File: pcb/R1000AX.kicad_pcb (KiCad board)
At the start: 4 copper layers, 175 x 65.5 mm, 133 parts, among them J1 PCIESOCKET-X1, J10 PCIESOCKET-X1, J11 PCIESOCKET-X1, J12 PCIESOCKET-X1, J13 PCIESOCKET-X1, J14 PCIESOCKET-X1, J15 PCIESOCKET-X1, J16 CONN127P-02X05, J17 USB_B_RECEPTACLE, J18 SOCKET254P-01X02, J2 PCIESOCKET-X1, J25 SOCKET420P-02X04-CPU, J3 PCIESOCKET-X1, J31 USB_A_RECEPTACLE_2, J4 PCIESOCKET-X1, J5 PCIESOCKET-X1, J6 PCIESOCKET-X1, J7 PCIESOCKET-X1, J8 PCIESOCKET-X1, J81 SOCKET254P-01X02, J82 SOCKET254P-01X02, J83 SOCKET254P-01X02, J9 PCIESOCKET-X1, Q1 DMG2305UX-7, Q2 PSMN1R2-30YLC, Q3 Q_PNP_BEC, Q4 Q_NPN_BEC, Q5 Q_PNP_BEC, Q6 Q_PNP_BEC, U1 LPC1769FBD100,551, U2 AP3418, U20 M24C08-FDW6TP, U3 BD9E302EFJ-E2, U4 INA3221AIRGVR, U5 LM5060MM/NOPB, Y1 XTAL4_12MHz

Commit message: updated silkscreen with RoHS
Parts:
- added A5: ART, Symbols:RoHS-Logo_6mm_SilkScreen, B.Cu at (165.4, 93.6)
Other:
- board text added: "EEPROM WRITE PROT"

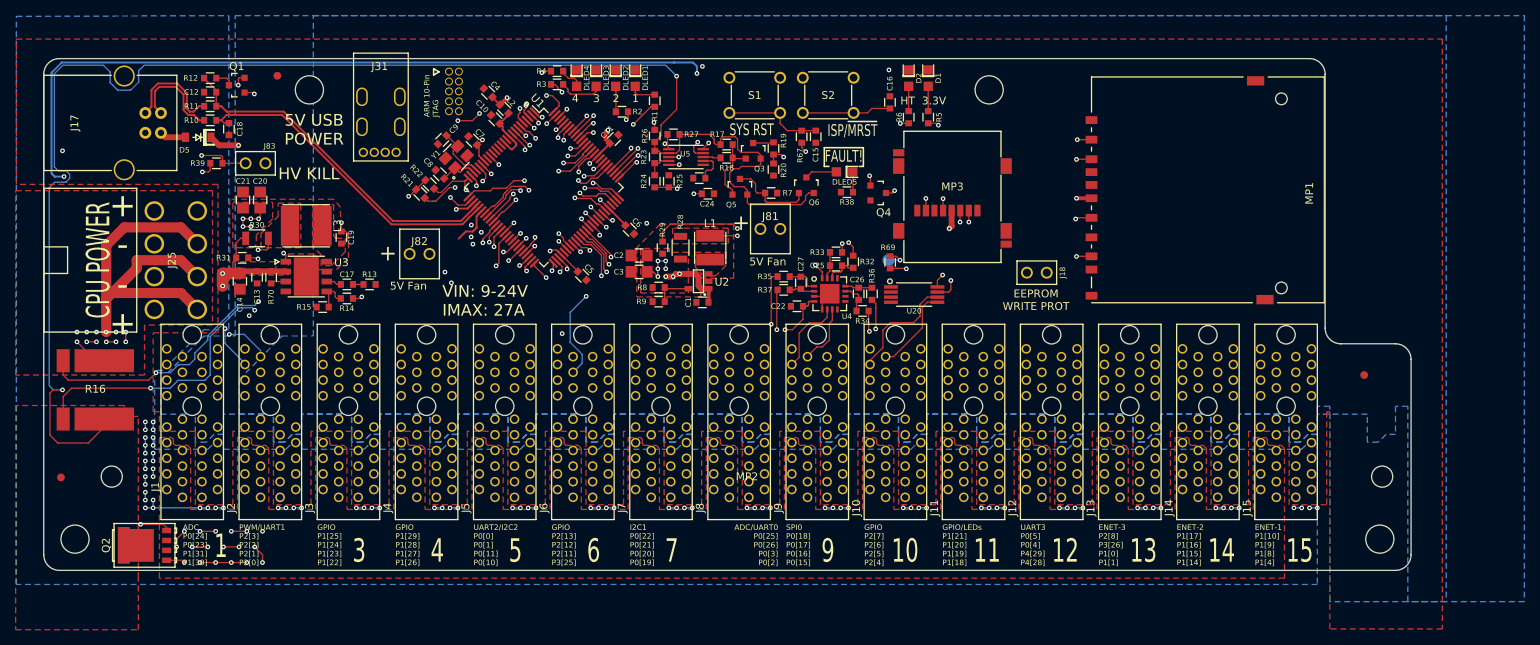
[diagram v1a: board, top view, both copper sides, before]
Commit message: added socket for CHIP and other compute modules
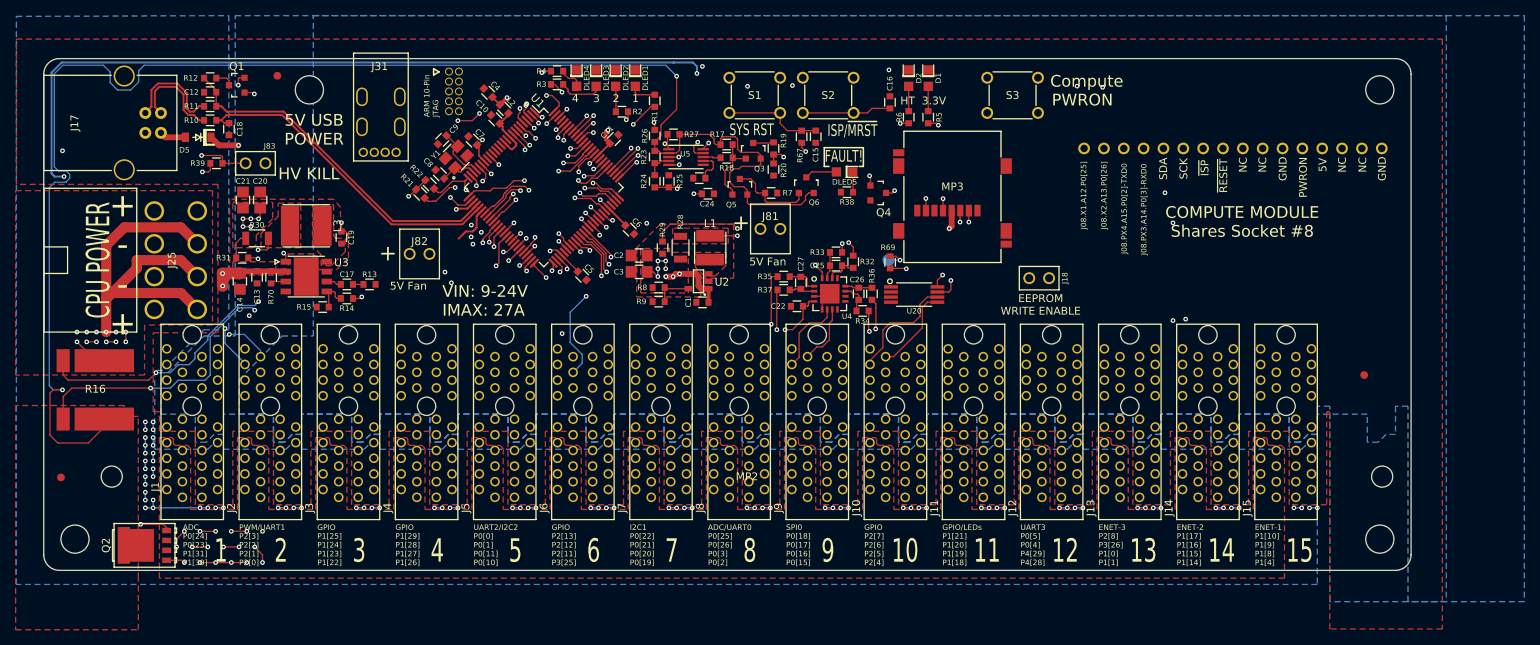
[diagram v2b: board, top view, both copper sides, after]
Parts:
- removed MP1: SDCARD_RECEPTACLE, Main:SDCARD_RECEPTACLE
- added J19: CHIPPRO, Main:CHIPPRO, F.Cu at (203.2, 85.0)
- added S3: SPST_PUSHBTN, Main:SPST_PUSHBTN, F.Cu at (175.0, 78.2)
- moved MP8 50.5 mm to (221.8, 85.8)
- moved A5 47.6 mm to (211.8, 104.0)
- moved A3 19.2 mm to (217.8, 94.0)
- moved A4 11.0 mm to (175.8, 93.2)
- moved A1 10.1 mm to (197.0, 94.0)
- moved J18 0.76 mm to (178.4, 101.6)
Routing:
- net J08.PX2.A13.P0[26]: track 63.3 -> 152.6 mm, vias 1 -> 2
- net J08.PX3.A14.P0[3]: track 60.7 -> 148.0 mm
- net J08.PX1.A12.P0[25]: track 63.9 -> 150.2 mm, vias 1 -> 2
- net /~RESET: track 48.9 -> 131.5 mm, vias 1 -> 2
- net J08.PX4.A15.P0[2]: track 65.1 -> 146.3 mm
- net ~MRESET: track 272.2 -> 329.1 mm, vias 3 -> 4
- net /PWRON: track 0.00 -> 48.4 mm
- net SCL0: track 253.9 -> 283.6 mm, vias 3 -> 5
- net SDA0: track 228.9 -> 258.3 mm, vias 2 -> 4
- net SD_SSEL: track 83.4 -> 59.0 mm, vias 3 -> 2
- net SD_MISO: track 73.0 -> 48.7 mm, vias 3 -> 2
- net SD_MOSI: track 74.0 -> 50.1 mm, vias 3 -> 2
- net SD_SCK: track 72.3 -> 52.1 mm, vias 3 -> 2
- net +3V3: track 56.6 -> 54.7 mm, vias 24 -> 23
- net /EE_~WC: track 26.9 -> 25.2 mm
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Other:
- outline, holes or cut-outs redrawn
- board text added: "8"
- board text added: "COMPUTE MODULE Shares Socket #8"
- board text added: "Compute"
- board text added: "EEPROM WRITE ENABLE"
- board text added: "PWRON"
- board text removed: "EEPROM WRITE PROT"

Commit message: completed layout with internet connected module, updated gerbers and bom
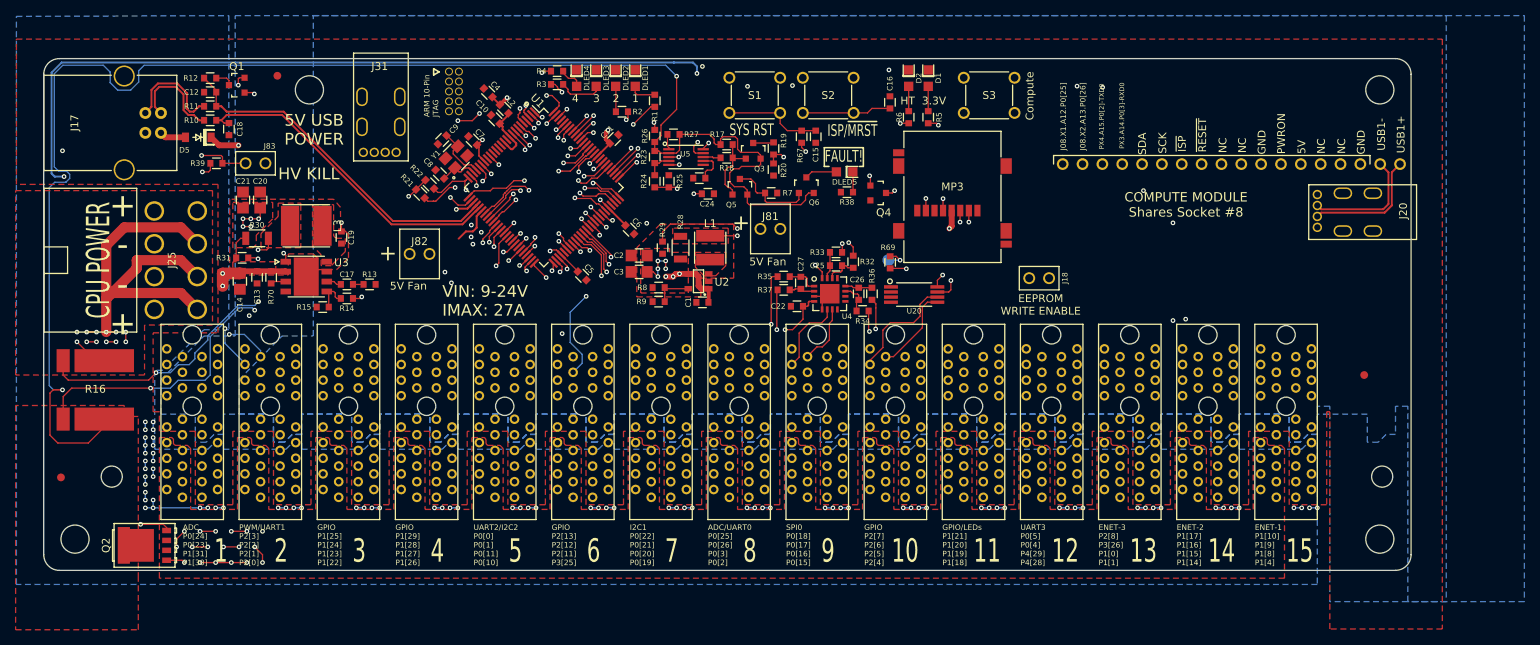
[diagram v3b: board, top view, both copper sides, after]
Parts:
- added J20: USB_A_RECEPTACLE_2, Main:USB_A_RECEPTACLE_2, F.Cu at (214.0, 93.0)
- J19: value CHIPPRO -> COMPUTE_MOD_1; footprint Main:CHIPPRO -> Main:COMPUTE_MOD_1
- MP2: value BRACKET-R1000A -> BRACKET-R1000AX; footprint Main:BRACKET-R1000A -> Main:BRACKET-R1000AX
- moved A3 61.5 mm to (156.4, 90.1)
- moved A5 26.0 mm to (198.8, 81.5)
- moved A4 6.64 mm to (170.5, 89.2)
- moved A1 4.51 mm to (198.0, 98.4)
- moved S3 3.00 mm to (172.0, 78.2)
- moved J19 2.01 mm to (203.0, 87.0)
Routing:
- net /COMPUTE_USB+: track 0.00 -> 15.8 mm
- net /COMPUTE_USB-: track 0.00 -> 15.1 mm
- net J08.PX2.A13.P0[26]: track 152.6 -> 155.6 mm
- net SCL0: track 283.6 -> 281.1 mm
- net J08.PX1.A12.P0[25]: track 150.2 -> 152.6 mm
- net /PWRON: track 48.4 -> 50.7 mm
- net SDA0: track 258.3 -> 258.9 mm
- net /~RESET: track 131.5 -> 130.9 mm
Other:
- board text removed: "PWRON"

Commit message: ensured distance margin between last module and host usb connector
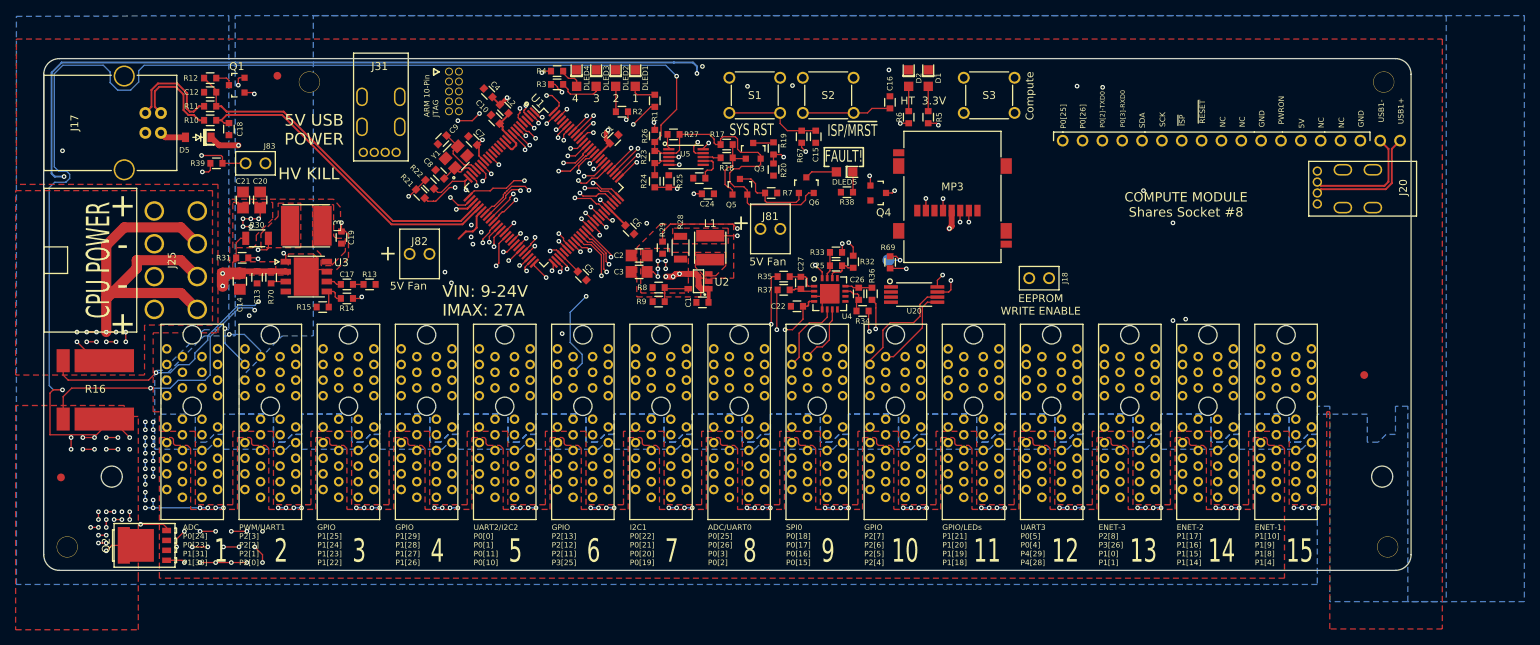
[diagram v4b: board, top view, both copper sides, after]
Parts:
- MP4, MP6, MP7, MP8: value MECH_NPTH_M4 -> MECH_NPTH_M3; footprint Main:MECH_NPTH_M4 -> Main:MECH_NPTH_M3
- moved A3 37.8 mm to (194.2, 91.4)
- moved A4 36.1 mm to (206.6, 90.4)
- moved A1 26.3 mm to (172.7, 91.5)
- moved A5 21.2 mm to (200.6, 102.6)
- moved MP7 7.81 mm to (49.0, 140.0)
- moved J19 3.00 mm to (203.0, 84.0)
- moved J20 3.00 mm to (214.0, 90.0)
- moved MP6 1.00 mm to (85.0, 76.5)
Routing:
- net PFET_D: track 202.4 -> 242.6 mm, vias 2 -> 32
- net HV_~PGD: track 160.7 -> 165.3 mm
- net SDA0: track 258.9 -> 262.0 mm
- net SCL0: track 281.1 -> 284.1 mm
- net ~MRESET: track 328.8 -> 325.8 mm
- net J08.PX3.A14.P0[3]: track 147.8 -> 144.8 mm
- net J08.PX2.A13.P0[26]: track 155.6 -> 152.6 mm
- net J08.PX1.A12.P0[25]: track 152.6 -> 149.6 mm
- net /PWRON: track 50.7 -> 47.7 mm
- net /~RESET: track 130.9 -> 127.9 mm
- net J08.PX4.A15.P0[2]: track 145.8 -> 142.8 mm
- net HT: track 366.9 -> 365.6 mm

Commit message: completed v1.3.1, implemented changes based on second crowdsupply update
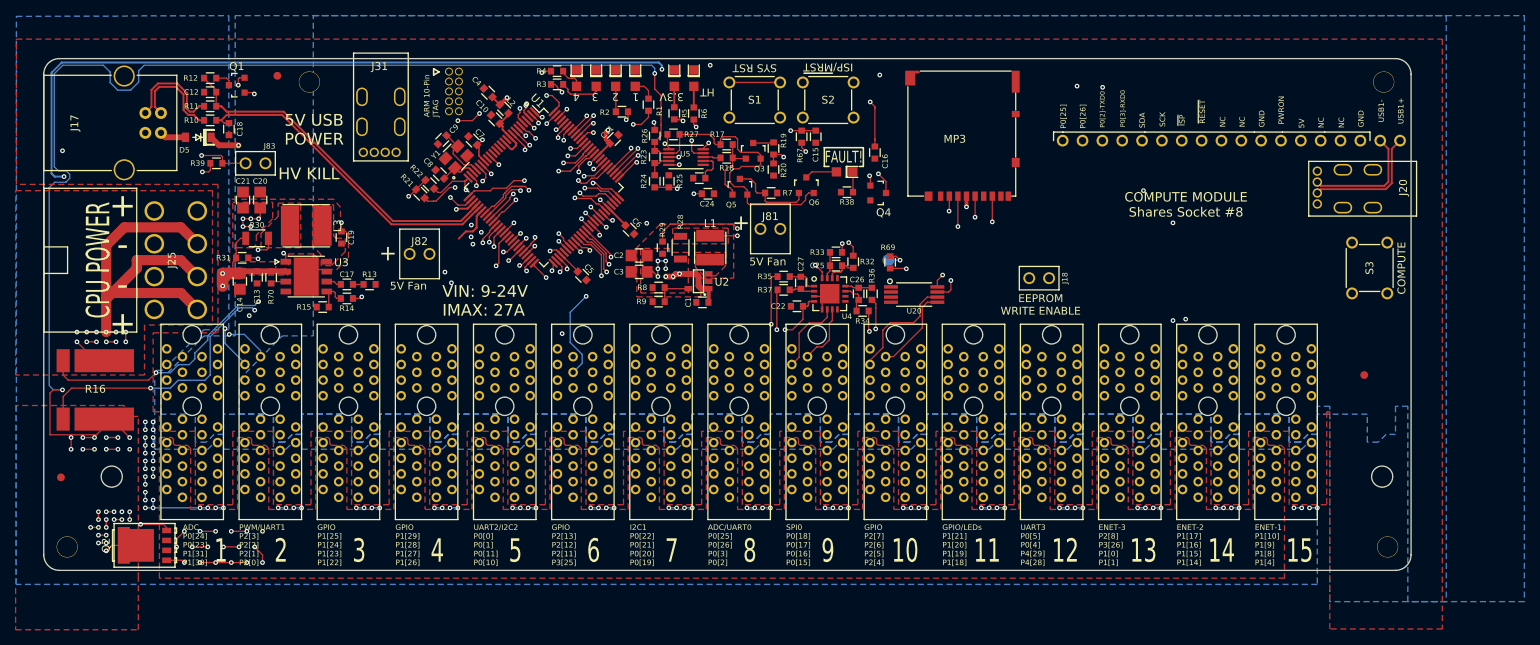
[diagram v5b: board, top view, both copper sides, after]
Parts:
- MP3: value MICROSD_SCHD3A0100 -> MICROSD_DM3AT-SF-PEJM5; footprint Main:CONN_SCHD3A0100 -> Main:MICROSD_RECEPTACLE_2
- moved S3 53.5 mm to (220.7, 100.3), turned to 270 degrees
- moved R5 32.5 mm to (131.7, 80.5)
- moved D1 32.5 mm to (131.7, 76.0)
- moved R6 27.5 mm to (134.2, 80.5)
- moved D2 27.5 mm to (134.2, 76.0)
- moved MP3 7.84 mm to (165.8, 90.5), turned to 180 degrees
- moved C16 6.71 mm to (157.4, 85.5), turned to 270 degrees
- moved R1 0.94 mm to (128.4, 79.4)
- moved S1 0.60 mm to (142.0, 78.8), turned to 0 degrees
- moved S2 0.60 mm to (151.4, 78.8), turned to 0 degrees
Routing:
- net HT: track 365.6 -> 331.2 mm
- net /PWRON: track 47.7 -> 36.0 mm
- net SD_MISO: track 48.7 -> 56.8 mm
- net SD_SSEL: track 59.0 -> 52.2 mm
- net HV_~PGD: track 165.3 -> 162.1 mm
- net SD_SCK: track 52.1 -> 55.0 mm
- net J08.PX3.A14.P0[3]: track 144.8 -> 142.0 mm
- net PFET_D: track 242.6 -> 239.9 mm
- net J08.PX4.A15.P0[2]: track 142.8 -> 140.1 mm
- net SD_MOSI: track 50.1 -> 52.3 mm
- net /~RESET: track 127.9 -> 130.1 mm
- net HV_EN: track 130.2 -> 128.5 mm
- net +3V3: track 54.7 -> 53.4 mm
- net J08.PX2.A13.P0[26]: track 152.6 -> 153.5 mm
- net J08.PX1.A12.P0[25]: track 149.6 -> 150.4 mm
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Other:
- board text added: "COMPUTE"
- board text added: "JuicyBoard - R1000AX v1.3.1 Designed by plugg.ee Labs LLC San Jose CA, USA http://plugg.ee"
- board text removed: "Compute"
- board text removed: "JuicyBoard - R1000AX v1.3 Designed by plugg.ee Labs LLC San Jose CA, USA http://plugg.ee"
